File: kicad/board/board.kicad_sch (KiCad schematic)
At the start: 71 parts, among them J0 Netz

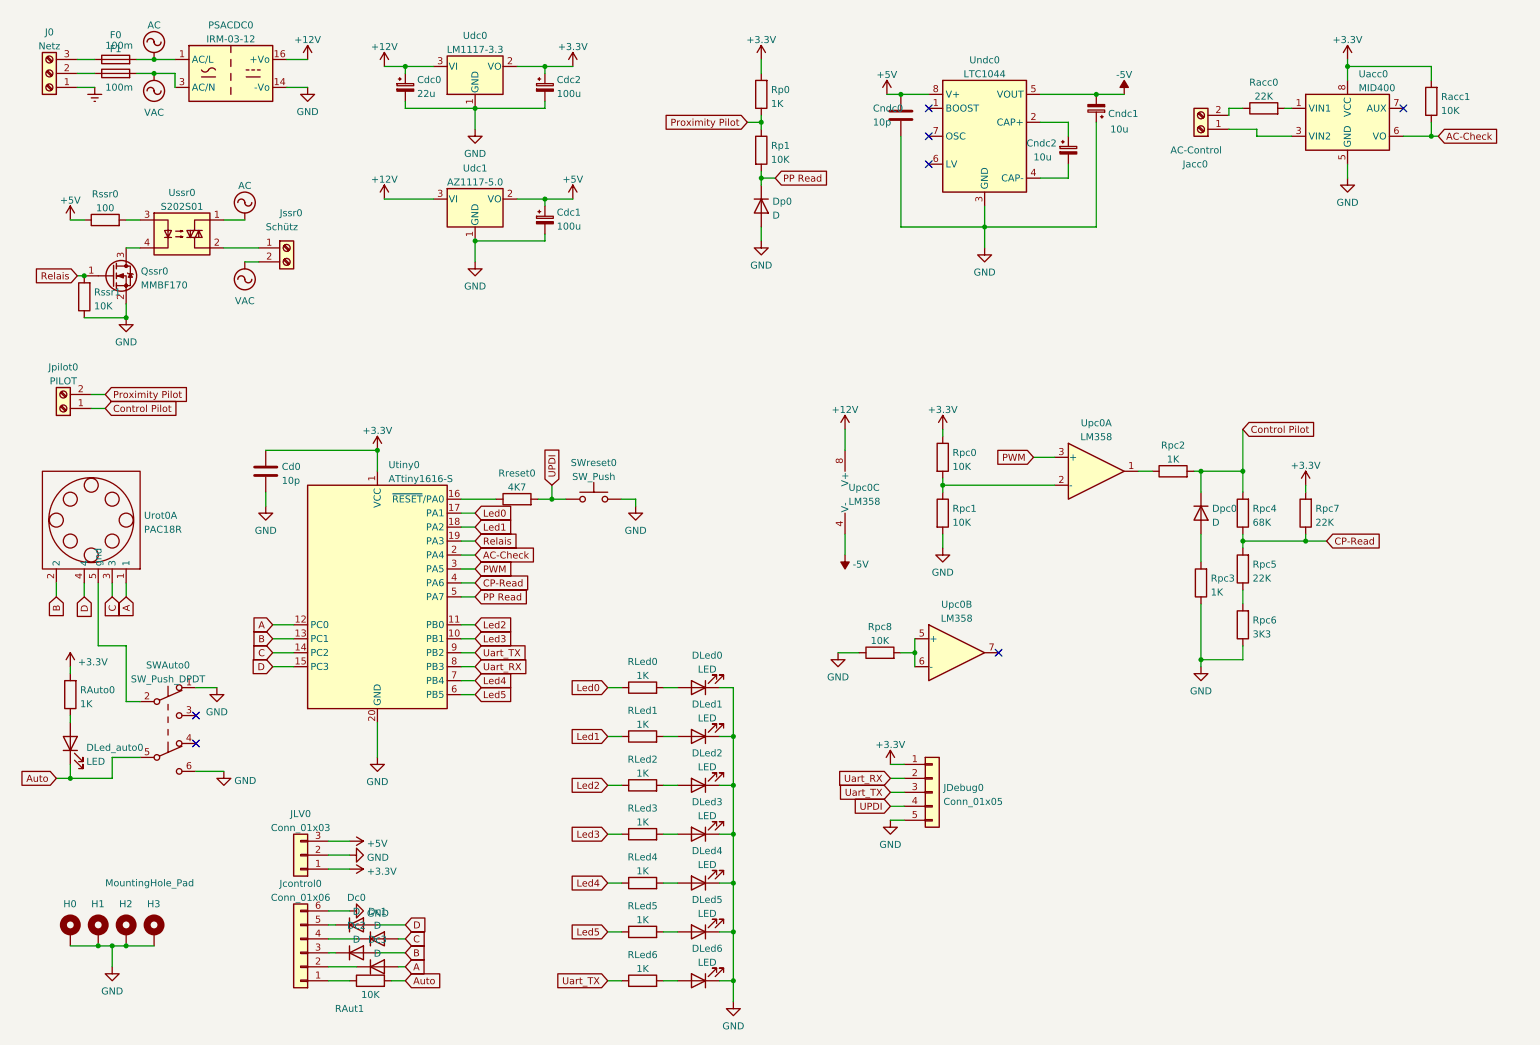
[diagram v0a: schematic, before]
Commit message: Hardware: PCB wie gefräst
Auf Fräsen  optimiert. d.h.:
-> Vias auf 1.6x1.0 mm vergrößert
-> An allen Pins die auf Vorderseite angebunden sind Löcher
   vergrößert (für Buchsen)

Probleme:
-> Falscher Footprint Solid state relais
-> Falscher Footprint 100uF Kondensatoren (2x)
-> Footprint für Drehschalter (PAC18) fehlerhaft
-> Schaltungsfehler: Drehschalter verhält sich umgekehrt als angenommen
-> Vorwiderstände für rote LEDs zu hoch
-> Reset-Knopf ohne Funktion
-> Spannungsabfall im OPV => PWM -3 ... +10 V
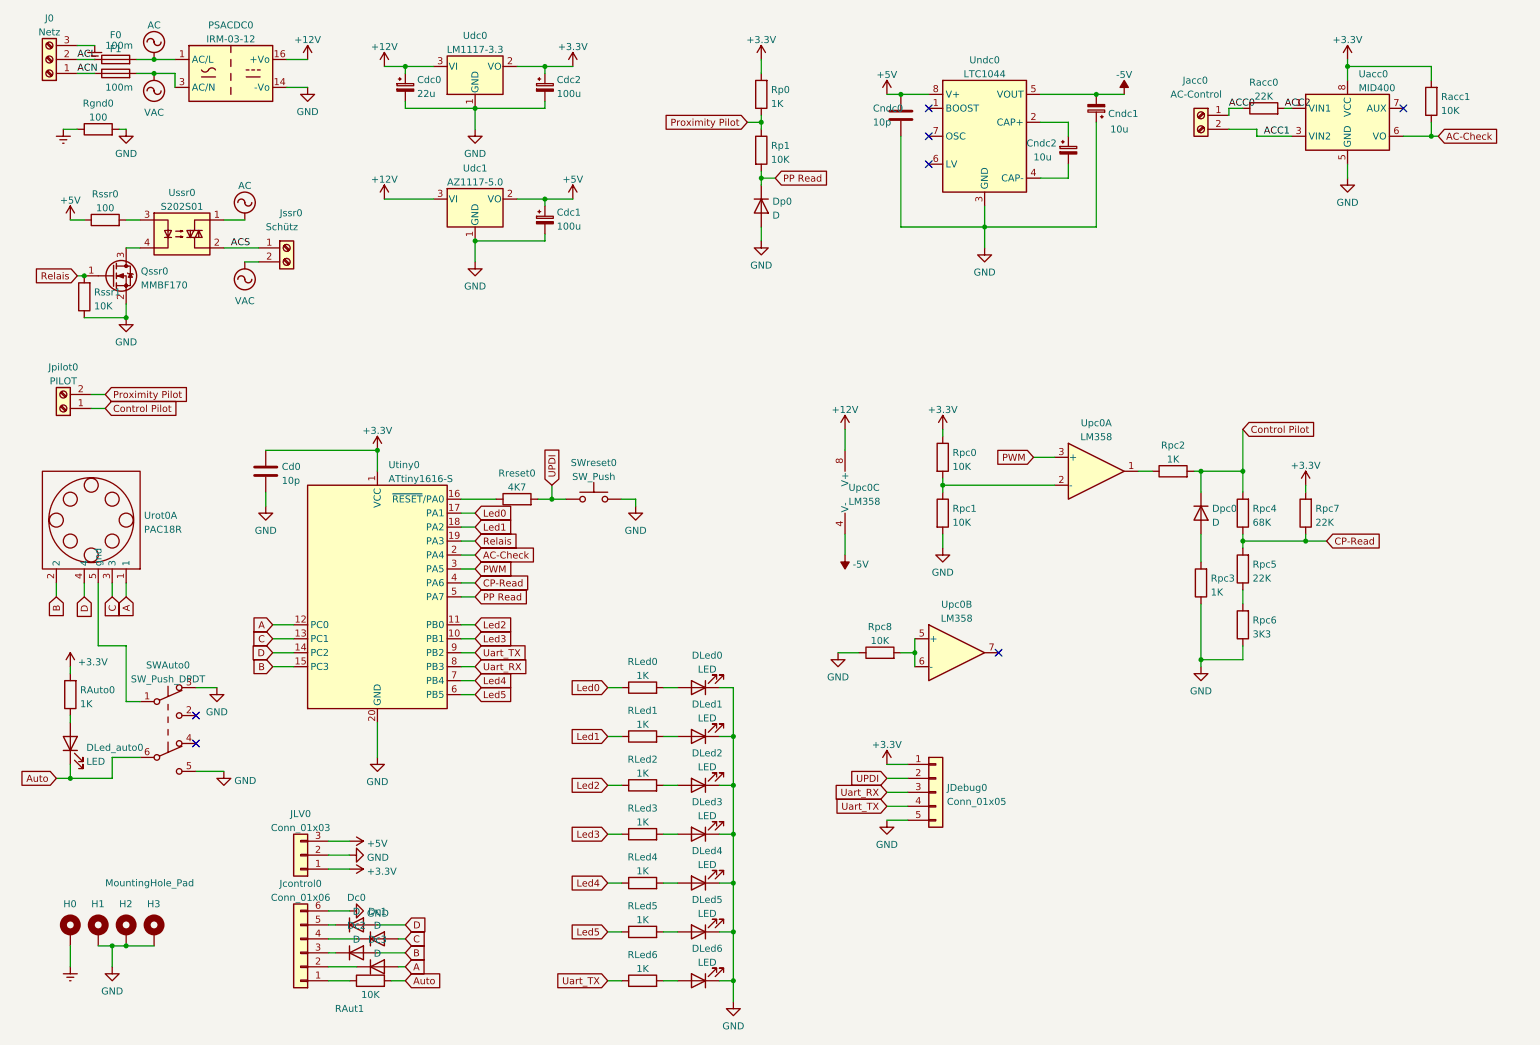
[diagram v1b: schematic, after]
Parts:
- added Rgnd0: 100, Resistor_SMD:R_1206_3216Metric, symbol Device:R
- Racc0: footprint Resistor_THT:R_Axial_DIN0207_L6.3mm_D2.5mm_P15.24mm_Horizontal -> Resistor_THT:R_Axial_DIN0207_L6.3mm_D2.5mm_P7.62mm_Horizontal
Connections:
- net Auto: now also SWAuto0.6 (C); no longer SWAuto0.5 (B)
- net B: now also Utiny0.15 (PC3); no longer Utiny0.13 (PC1)
- net C: now also Utiny0.13 (PC1); no longer Utiny0.14 (PC2)
- net D: now also Utiny0.14 (PC2); no longer Utiny0.15 (PC3)
- net Earth: now also H0.1, J0.3 (Pin_3), Rgnd0.1; no longer J0.1 (Pin_1)
- net GND: now also SWAuto0.3 (C), SWAuto0.5 (B), Rgnd0.2; no longer H0.1, SWAuto0.1 (A), SWAuto0.6 (C)
- net UPDI: now also JDebug0.2 (Pin_2); no longer JDebug0.4 (Pin_4)
- net Uart_RX: now also JDebug0.3 (Pin_3); no longer JDebug0.2 (Pin_2)
- net Uart_TX: now also JDebug0.4 (Pin_4); no longer JDebug0.3 (Pin_3)
- net ACC2: now reaches Racc0.2, Uacc0.1 (VIN1)
- net ACC0: now reaches Jacc0.1 (Pin_1)
- net ACC0: now also Racc0.1; no longer Uacc0.3 (VIN2)
- net at Urot0.5 (gnd): now also SWAuto0.1 (A); no longer SWAuto0.2 (B)
- net ACS: now reaches Jssr0.1 (Pin_1), Ussr0.2
- net ACC1: now reaches Jacc0.2 (Pin_2)
- net ACC1: now also Uacc0.3 (VIN2); no longer Racc0.1
- net ACL: now reaches J0.2 (Pin_2)
- net ACL: now also F0.1; no longer F1.1
- new net ACN: F1.1, J0.1 (Pin_1)
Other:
- moved on the sheet: J0, JDebug0, Jacc0

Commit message: hardware: kicad board bestellt
simplifiziert:
Strom sowie Fehlerstrom werden durch Hauptsicherung und FI gesichert.
AC-Check is a recht sinnlos weil gegen ein hängendes Relais kannst
eh nit viel tun.
Diodencheck macht sinn, wird auch mit -5V statt den Spezifizierten -12V
duchgeführt, sollt genauso funktionieren, meine LTC1044 halten max 9V aus.
Rechtck-Puls wird mit Transistor-Brücke realisiert (simuliert, nicht
getestet). Steigende Flanke wird begrenzt durch pull-down Widerstand
(auf -5V) und parasitic capazity.
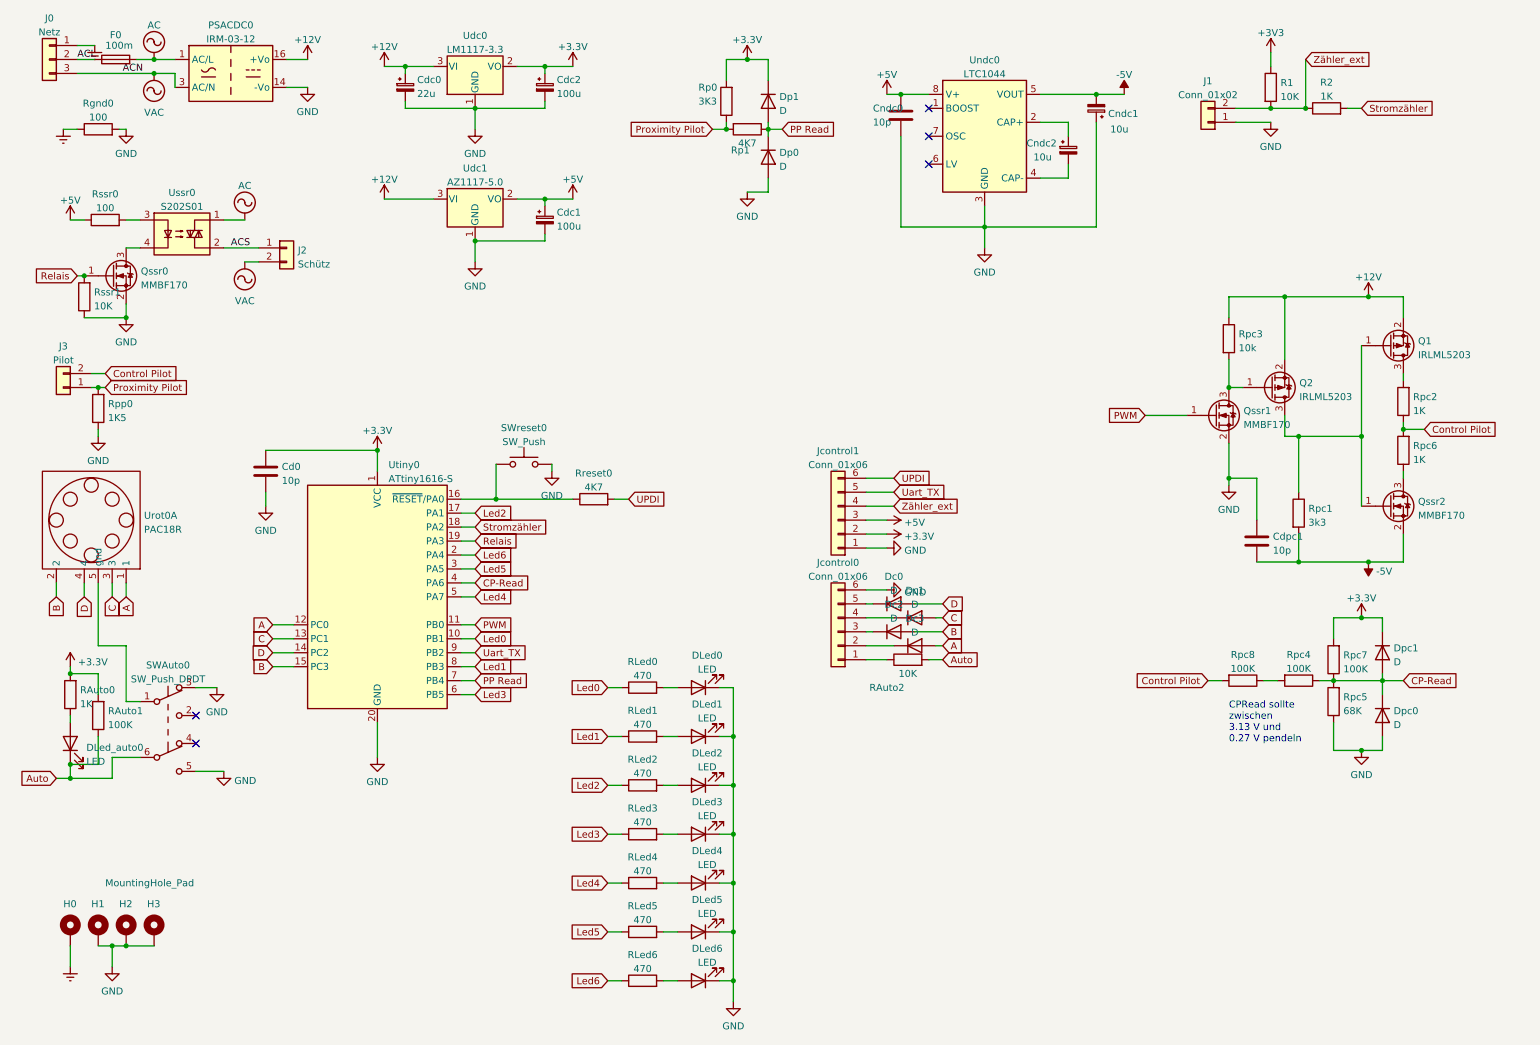
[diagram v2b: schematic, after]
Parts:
- removed F1: 100m, Fuse:Fuse_Littelfuse_372_D8.50mm, symbol Device:Fuse
- removed J0: Netz, TerminalBlock:TerminalBlock_bornier-3_P5.08mm, symbol Connector:Screw_Terminal_01x03
- removed JDebug0: Conn_01x05, Connector_JST:JST_PH_B5B-PH-K_1x05_P2.00mm_Vertical, symbol Connector_Generic:Conn_01x05
- removed JLV0: Conn_01x03, Connector_Molex:Molex_KK-254_AE-6410-03A_1x03_P2.54mm_Vertical, symbol Connector_Generic:Conn_01x03
- removed Jacc0: AC-Control, TerminalBlock:TerminalBlock_bornier-2_P5.08mm, symbol Connector:Screw_Terminal_01x02
- removed Jpilot0: PILOT, TerminalBlock:TerminalBlock_bornier-2_P5.08mm, symbol Connector:Screw_Terminal_01x02
- removed Jssr0: Schütz, TerminalBlock:TerminalBlock_bornier-2_P5.08mm, symbol Connector:Screw_Terminal_01x02
- removed Racc0: 22K, Resistor_THT:R_Axial_DIN0207_L6.3mm_D2.5mm_P7.62mm_Horizontal, symbol Device:R
- removed Racc1, Rpc0: 10K, Resistor_SMD:R_1206_3216Metric, symbol Device:R
- removed Uacc0: MID400, Package_DIP:DIP-8_W7.62mm, symbol Isolator:MID400
- removed Upc0: LM358, Package_SO:SOIC-8_3.9x4.9mm_P1.27mm, symbol Amplifier_Operational:LM358
- added Cdpc1: 10p, Capacitor_SMD:C_1206_3216Metric, symbol Device:C
- added Dp1, Dpc1: D, Diode_SMD:D_1206_3216Metric, symbol Device:D
- added J0: Netz, Connector_Phoenix_MC_HighVoltage:PhoenixContact_MC_1,5_3-G-5.08_1x03_P5.08mm_Horizontal, symbol Connector_Generic:Conn_01x03
- added J1: Conn_01x02, Connector_Phoenix_MC:PhoenixContact_MC_1,5_2-G-3.5_1x02_P3.50mm_Horizontal, symbol Connector_Generic:Conn_01x02
- added J2: Schütz, Connector_Phoenix_MC:PhoenixContact_MC_1,5_2-G-3.5_1x02_P3.50mm_Horizontal, symbol Connector_Generic:Conn_01x02
- added J3: Pilot, Connector_Phoenix_MC:PhoenixContact_MC_1,5_2-G-3.5_1x02_P3.50mm_Horizontal, symbol Connector_Generic:Conn_01x02
- added Jcontrol1: Conn_01x06, Connector_JST:JST_XH_B6B-XH-AM_1x06_P2.50mm_Vertical, symbol Connector_Generic:Conn_01x06
- added Q1, Q2: IRLML5203, Package_TO_SOT_SMD:SOT-23, symbol Transistor_FET:IRLML5203
- added Qssr1, Qssr2: MMBF170, Package_TO_SOT_SMD:SOT-23, symbol Transistor_FET:MMBF170
- added R1: 10K, Resistor_SMD:R_1206_3216Metric, symbol Device:R
- added R2: 1K, Resistor_SMD:R_1206_3216Metric, symbol Device:R
- added RAuto1: 100K, Resistor_SMD:R_1206_3216Metric, symbol Device:R
- added Rpp0: 1K5, Resistor_THT:R_Axial_DIN0207_L6.3mm_D2.5mm_P7.62mm_Horizontal, symbol Device:R
- Cdc1, Cdc2: footprint Capacitor_Tantalum_SMD:CP_EIA-3216-12_Kemet-S -> Capacitor_THT:CP_Radial_D6.3mm_P2.50mm
- Jcontrol0: footprint Connector_Molex:Molex_KK-254_AE-6410-06A_1x06_P2.54mm_Vertical -> Connector_JST:JST_XH_B6B-XH-AM_1x06_P2.50mm_Vertical
- RLed0, RLed1, RLed2, RLed3, RLed4, RLed5, RLed6: value 1K -> 470
- Rp0: value 1K -> 3K3
- Rp1: value 10K -> 4K7
- Rpc1: value 10K -> 3k3
- Rpc3: value 1K -> 10k
- Rpc4: value 68K -> 100K
- Rpc5: value 22K -> 68K
- Rpc6: value 3K3 -> 1K
- Rpc7: value 22K -> 100K
- Rpc8: value 10K -> 100K
- renumbered RAut1 to RAuto2
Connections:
- net Uart_RX is gone; now on net Led1: Utiny0.8 (PB3)
- net +12V: now also Rpc3.1, Q1.2 (S), Q2.2 (S)
- net +3V3: now also Dp1.1 (K), Dpc1.1 (K), Jcontrol1.2 (Pin_2), R1.1, RAuto1.2
- net +5V: now also Jcontrol1.3 (Pin_3)
- net -5V: now also Rpc1.2, Cdpc1.2, Qssr2.2 (S)
- net ACL: now also J0.2 (Pin_2)
- net ACS: now also J2.1 (Pin_1)
- net Auto: now also RAuto1.1
- net CP-Read: now also Dpc0.1 (K), Dpc1.2 (A)
- net Control Pilot: now also Rpc2.1, Rpc6.2, Rpc8.2, J3.2 (Pin_2); no longer Dpc0.1 (K), Rpc2.2, Rpc4.2
- net Earth: now also J0.1 (Pin_1)
- net GND: now also Dpc0.2 (A), Rpc5.1, Cdpc1.1, J1.1 (Pin_1), Jcontrol1.1 (Pin_1), Qssr1.2 (S), Rpp0.1; no longer Rpc1.2, Rpc3.1, Rpc6.1, Rpc8.1
- net Led0: now also Utiny0.10 (PB1); no longer Utiny0.17 (PA1)
- net Led1: no longer Utiny0.18 (PA2)
- net Led2: now also Utiny0.17 (PA1); no longer Utiny0.11 (PB0)
- net Led3: now also Utiny0.6 (PB5); no longer Utiny0.10 (PB1)
- net Led4: now also Utiny0.5 (PA7); no longer Utiny0.7 (PB4)
- net Led5: now also Utiny0.3 (PA5); no longer Utiny0.6 (PB5)
- net PP Read: now also Rp1.1, Utiny0.7 (PB4), Dp1.2 (A); no longer Rp1.2, Utiny0.5 (PA7)
- net PWM: now also Utiny0.11 (PB0), Qssr1.1 (G); no longer Utiny0.3 (PA5)
- net Proximity Pilot: now also Rp1.2, J3.1 (Pin_1), Rpp0.2; no longer Rp1.1
- net UPDI: now also Jcontrol1.6 (Pin_6); no longer SWreset0.1
- net Uart_TX: now also Jcontrol1.5 (Pin_5); no longer RLed6.1
- net VAC: now also J0.3 (Pin_3), J2.2 (Pin_2)
- net at Rpc1.1: now also Q1.1 (G), Q2.3 (D), Qssr2.1 (G)
- net at Rreset0.1, Utiny0.16 (~{RESET}/PA0): now also SWreset0.1
- net at Rpc3.2: now also Q2.1 (G), Qssr1.3 (D); no longer Dpc0.2 (A)
- net AC-Check renamed Led6
- net Led6: now also RLed6.1
- new net: Rpc4.2, Rpc8.1
- new net: Qssr2.3 (D), Rpc6.1
- new net: Q1.3 (D), Rpc2.2
- new net Stromzähler: R2.2, Utiny0.18 (PA2)
- new net Zähler_ext: J1.2 (Pin_2), Jcontrol1.4 (Pin_4), R1.2, R2.1
- no-connect marks 7 -> 5
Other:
- note added: "CPRead sollte zwischen 3.13 V und 0.27 V pendeln"
- moved on the sheet: Dc0, Dc1, Dc2, Dc3, Dp0, Dpc0, Jcontrol0, RAuto2, Rp0, Rpc1, Rpc2, Rpc4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
